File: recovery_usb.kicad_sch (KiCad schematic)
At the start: 47 parts, among them J3 USB-C_WE_632723300011, Q15 PJE138K, Q19 PJE138K, U23 AP22615A_TSOT26, U26 TPD4E05U06QDQARQ1, U56 HD3SS3220IRNHR, U57 TPD4E05U06QDQARQ1, U58 TPD4E05U06QDQARQ1

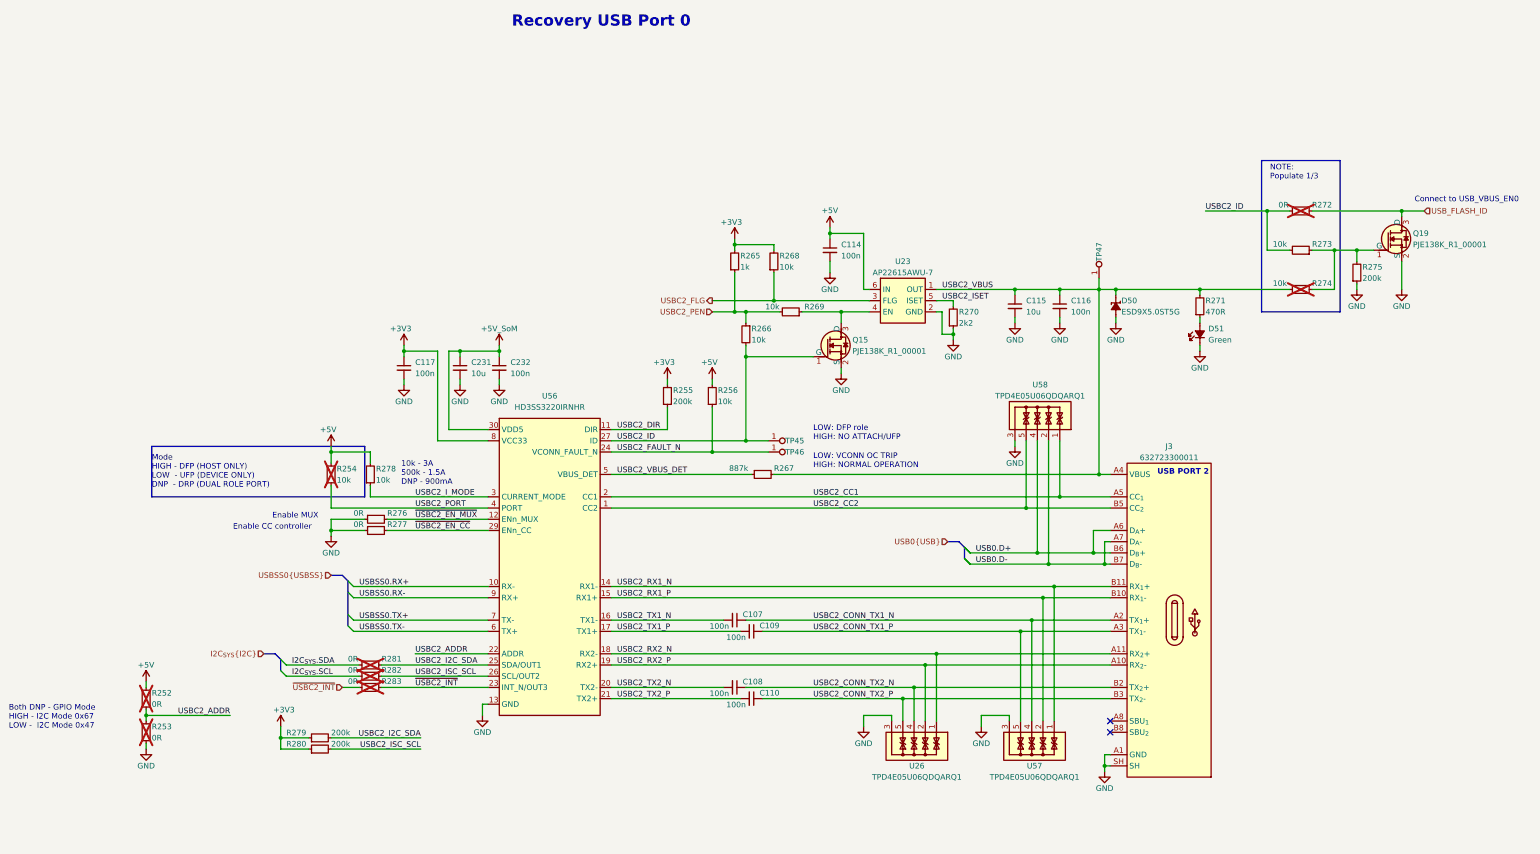
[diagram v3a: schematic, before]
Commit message: [#82837] Finish mapping PCIe and SFP+ connections on SoM
[#82837] WIP: correct ERC errors

[#82837] WIP: correct ERC errors, fix signal direction of most buses

[#82837] Fix all ERC errors
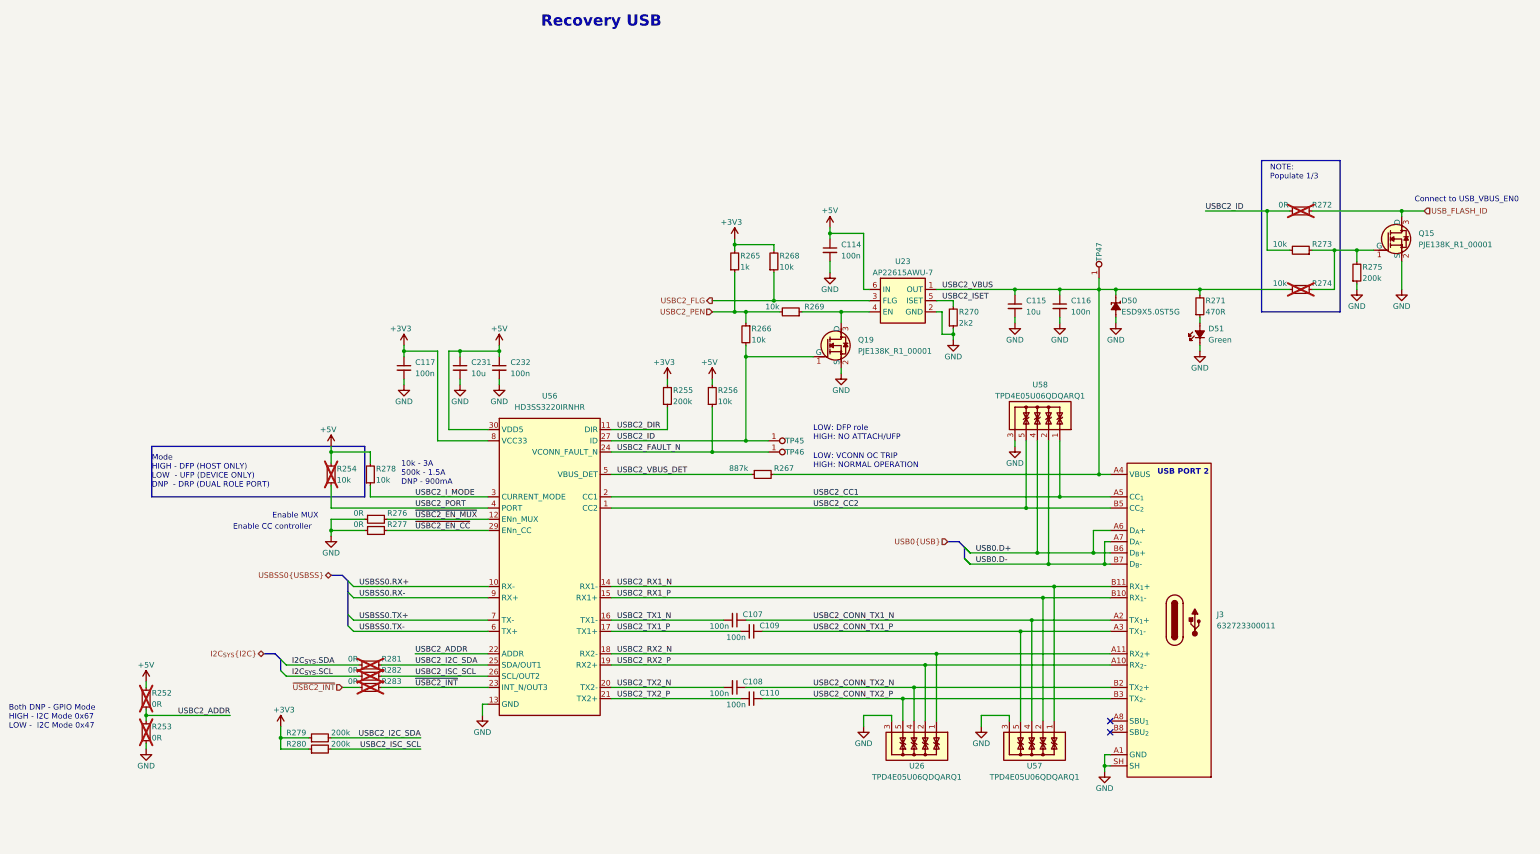
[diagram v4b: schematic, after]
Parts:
- Q15, Q19: now left out of the parts list
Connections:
- net +5V_SoM is gone; now on net +5V: C231.1, C232.1, U56.30 (VDD5)
- net USBC2_ID: now also Q19.1 (G); no longer Q15.1 (G)
- net USB_FLASH_ID: now also Q15.3 (D); no longer Q19.3 (D)
- net at R269.1, U23.4 (EN): now also Q19.3 (D); no longer Q15.3 (D)
- net at R273.1, R274.1, R275.2: now also Q15.1 (G); no longer Q19.1 (G)
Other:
- note added: "Recovery USB"
- note removed: "Recovery USB Port 0"

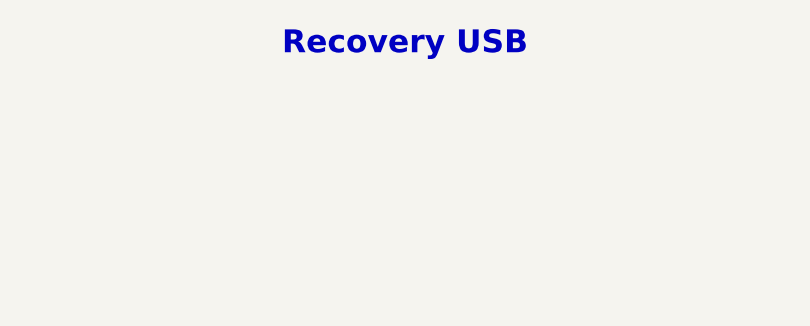
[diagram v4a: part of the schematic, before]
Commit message: [#83224] Import all of the components to PCB and divide them into functional groups
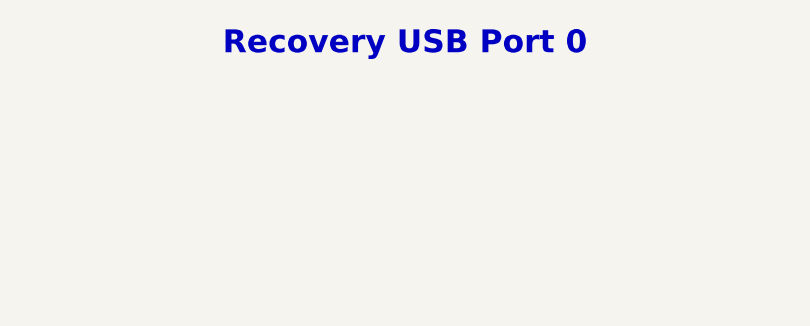
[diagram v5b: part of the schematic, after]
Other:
- note added: "Recovery USB Port 0"
- note removed: "Recovery USB"
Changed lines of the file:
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@@
 		)
 	)
-	(text "Recovery USB"
+	(text "Recovery USB Port 0\n"
 		(exclude_from_sim no)
 		(at 185.674 24.384 0)

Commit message: [#83224] Start placing USB
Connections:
- net USB0.D+: now also J3.A7 (D_{A}-), J3.B7 (D_{B}-); no longer J3.A6 (D_{A}+), J3.B6 (D_{B}+)
- net USB0.D-: now also J3.A6 (D_{A}+), J3.B6 (D_{B}+); no longer J3.A7 (D_{A}-), J3.B7 (D_{B}-)
- net USBC2_RX1_N: now also J3.B10 (RX_{1}-); no longer J3.B11 (RX_{1}+)
- net USBC2_RX1_P: now also J3.B11 (RX_{1}+); no longer J3.B10 (RX_{1}-)
- net USBC2_RX2_N: now also J3.A10 (RX_{2}-); no longer J3.A11 (RX_{2}+)
- net USBC2_RX2_P: now also J3.A11 (RX_{2}+); no longer J3.A10 (RX_{2}-)
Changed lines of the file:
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@@
+	)
+	(junction
+		(at 298.45 144.78)
+		(diameter 0)
+		(color 0 0 0 0)
 	)
 	(junction
@@
 	(junction
 		(at 265.43 95.25)
-		(diameter 0)
-		(color 0 0 0 0)
-	)
-	(junction
-		(at 297.18 144.78)
 		(diameter 0)
 		(color 0 0 0 0)
@@
 	(wire
 		(pts
-			(xy 288.29 152.4) (xy 300.99 152.4)
+			(xy 288.29 152.4) (xy 292.1 152.4)
 		)
 		(stroke
@@
 	(wire
 		(pts
+			(xy 292.1 147.32) (xy 294.64 144.78)
+		)
+		(stroke
+			(width 0)
+			(type default)
+		)
+	)
+	(wire
+		(pts
 			(xy 218.44 90.17) (xy 226.06 90.17)
 		)
@@
 	(wire
 		(pts
+			(xy 294.64 154.94) (xy 300.99 154.94)
+		)
+		(stroke
+			(width 0)
+			(type default)
+		)
+	)
+	(wire
+		(pts
 			(xy 162.56 105.41) (xy 162.56 106.68)
 		)
@@
 	(wire
 		(pts
-			(xy 285.75 154.94) (xy 300.99 154.94)
-		)
-		(stroke
-			(width 0)
-			(type default)
-		)
-	)
-	(wire
-		(pts
-			(xy 300.99 139.7) (xy 297.18 139.7)
+			(xy 285.75 154.94) (xy 292.1 154.94)
+		)
+		(stroke
+			(width 0)
+			(type default)
+		)
+	)
+	(wire
+		(pts
+			(xy 300.99 139.7) (xy 298.45 139.7)
 		)
 		(stroke
@@
 	(wire
 		(pts
+			(xy 294.64 152.4) (xy 300.99 152.4)
+		)
+		(stroke
+			(width 0)
+			(type default)
+		)
+	)
+	(wire
+		(pts
 			(xy 129.54 154.94) (xy 160.02 154.94)
 		)
@@
 	(wire
 		(pts
+			(xy 294.64 167.64) (xy 300.99 167.64)
+		)
+		(stroke
+			(width 0)
+			(type default)
+		)
+	)
+	(wire
+		(pts
 			(xy 245.11 184.15) (xy 245.11 181.61)
 		)
@@
 	(wire
 		(pts
+			(xy 294.64 144.78) (xy 298.45 144.78)
+		)
+		(stroke
+			(width 0)
+			(type default)
+		)
+	)
+	(wire
+		(pts
 			(xy 187.96 116.84) (xy 200.66 116.84)
 		)
@@
 	(wire
 		(pts
+			(xy 292.1 167.64) (xy 294.64 170.18)
+		)
+		(stroke
+			(width 0)
+			(type default)
+		)
+	)
+	(wire
+		(pts
 			(xy 187.96 175.26) (xy 213.36 175.26)
 		)
@@
 	(wire
 		(pts
-			(xy 259.08 170.18) (xy 300.99 170.18)
+			(xy 259.08 170.18) (xy 292.1 170.18)
 		)
 		(stroke
@@
 	(wire
 		(pts
+			(xy 292.1 144.78) (xy 294.64 147.32)
+		)
+		(stroke
+			(width 0)
+			(type default)
+		)
+	)
+	(wire
+		(pts
 			(xy 144.78 186.69) (xy 124.46 186.69)
 		)
@@
 	(wire
 		(pts
-			(xy 287.02 147.32) (xy 299.72 147.32)
+			(xy 287.02 147.32) (xy 292.1 147.32)
 		)
 		(stroke
@@
 	(wire
 		(pts
+			(xy 292.1 170.18) (xy 294.64 167.64)
+		)
+		(stroke
+			(width 0)
+			(type default)
+		)
+	)
+	(wire
+		(pts
 			(xy 114.3 172.72) (xy 130.81 172.72)
 		)
@@
 	(wire
 		(pts
+			(xy 294.64 170.18) (xy 300.99 170.18)
+		)
+		(stroke
+			(width 0)
+			(type default)
+		)
+	)
+	(wire
+		(pts
 			(xy 187.96 160.02) (xy 213.36 160.02)
 		)
@@
 	(wire
 		(pts
+			(xy 294.64 147.32) (xy 299.72 147.32)
+		)
+		(stroke
+			(width 0)
+			(type default)
+		)
+	)
+	(wire
+		(pts
 			(xy 143.51 167.64) (xy 160.02 167.64)
 		)
@@
 	(wire
 		(pts
+			(xy 292.1 152.4) (xy 294.64 154.94)
+		)
+		(stroke
+			(width 0)
+			(type default)
+		)
+	)
+	(wire
+		(pts
 			(xy 288.29 152.4) (xy 288.29 182.88)
 		)
@@
 	(wire
 		(pts
-			(xy 297.18 144.78) (xy 300.99 144.78)
-		)
-		(stroke
-			(width 0)
-			(type default)
-		)
-	)
-	(wire
-		(pts
 			(xy 302.26 86.36) (xy 302.26 85.09)
 		)
@@
 	(wire
 		(pts
-			(xy 297.18 139.7) (xy 297.18 144.78)
+			(xy 298.45 139.7) (xy 298.45 144.78)
 		)
 		(stroke
@@
 	(wire
 		(pts
-			(xy 284.48 144.78) (xy 297.18 144.78)
+			(xy 284.48 144.78) (xy 292.1 144.78)
 		)
 		(stroke
@@
 	(wire
 		(pts
+			(xy 292.1 154.94) (xy 294.64 152.4)
+		)
+		(stroke
+			(width 0)
+			(type default)
+		)
+	)
+	(wire
+		(pts
 			(xy 210.82 90.17) (xy 215.9 90.17)
 		)
@@
 	(wire
 		(pts
-			(xy 261.62 167.64) (xy 300.99 167.64)
+			(xy 261.62 167.64) (xy 292.1 167.64)
 		)
 		(stroke
@@
 		)
 		(stroke
+			(width 0)
+			(type default)
+		)
+	)
+	(wire
+		(pts
+			(xy 298.45 144.78) (xy 300.99 144.78)
+		)
+		(stroke

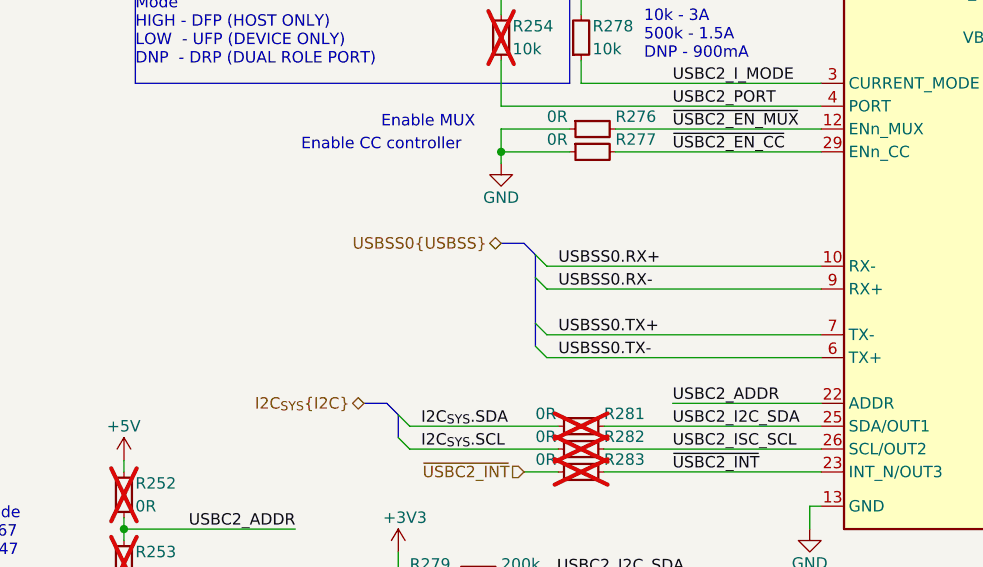
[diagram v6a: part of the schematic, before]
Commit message: [#83224] Add AC coupling capacitors to USBSS
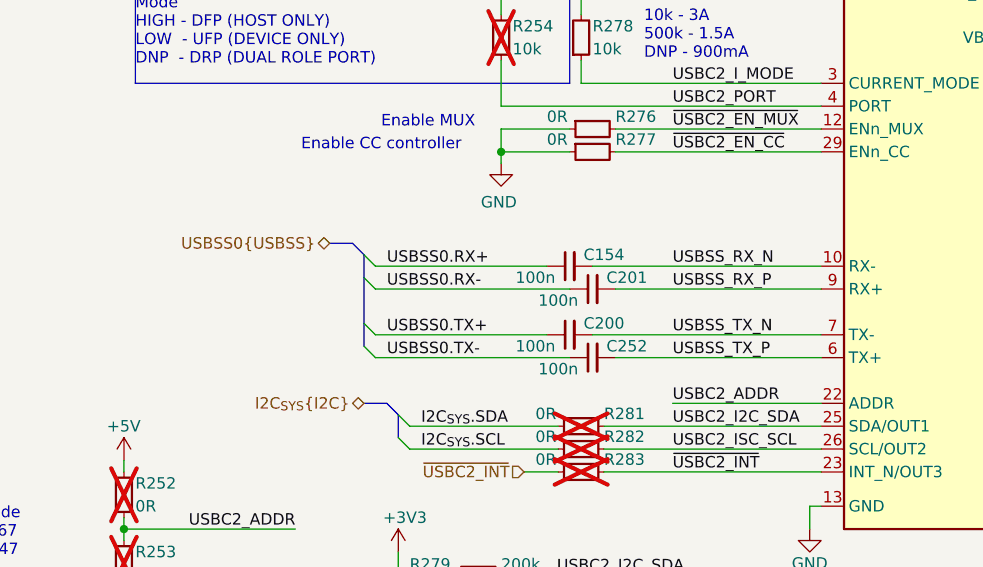
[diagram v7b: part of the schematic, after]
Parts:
- added C154, C200, C201, C252: C_100n_0402, antmicro-footprints:C_0402_1005Metric, symbol antmicroCapacitors0402:C_100n_0402
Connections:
- net USBSS0.RX+: now also C154.1; no longer U56.10 (RX-)
- net USBSS0.RX-: now also C201.1; no longer U56.9 (RX+)
- net USBSS0.TX+: now also C200.1; no longer U56.7 (TX-)
- net USBSS0.TX-: now also C252.1; no longer U56.6 (TX+)
- new net USBSS_RX_N: C154.2, U56.10 (RX-)
- new net USBSS_RX_P: C201.2, U56.9 (RX+)
- new net USBSS_TX_N: C200.2, U56.7 (TX-)
- new net USBSS_TX_P: C252.2, U56.6 (TX+)
